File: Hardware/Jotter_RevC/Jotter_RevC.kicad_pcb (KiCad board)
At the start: 2 copper layers, 76.2 x 76.2 mm, 44 parts, among them CON1 SD_Card, P1 USB_A, P2 CONN_01X02, P3 CONN_01X02, Q1 BSS138, Q2 BSS138, SW1 SPST, U1 ATSAMD11D14A, U10 APA102C, U2 MCP73831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

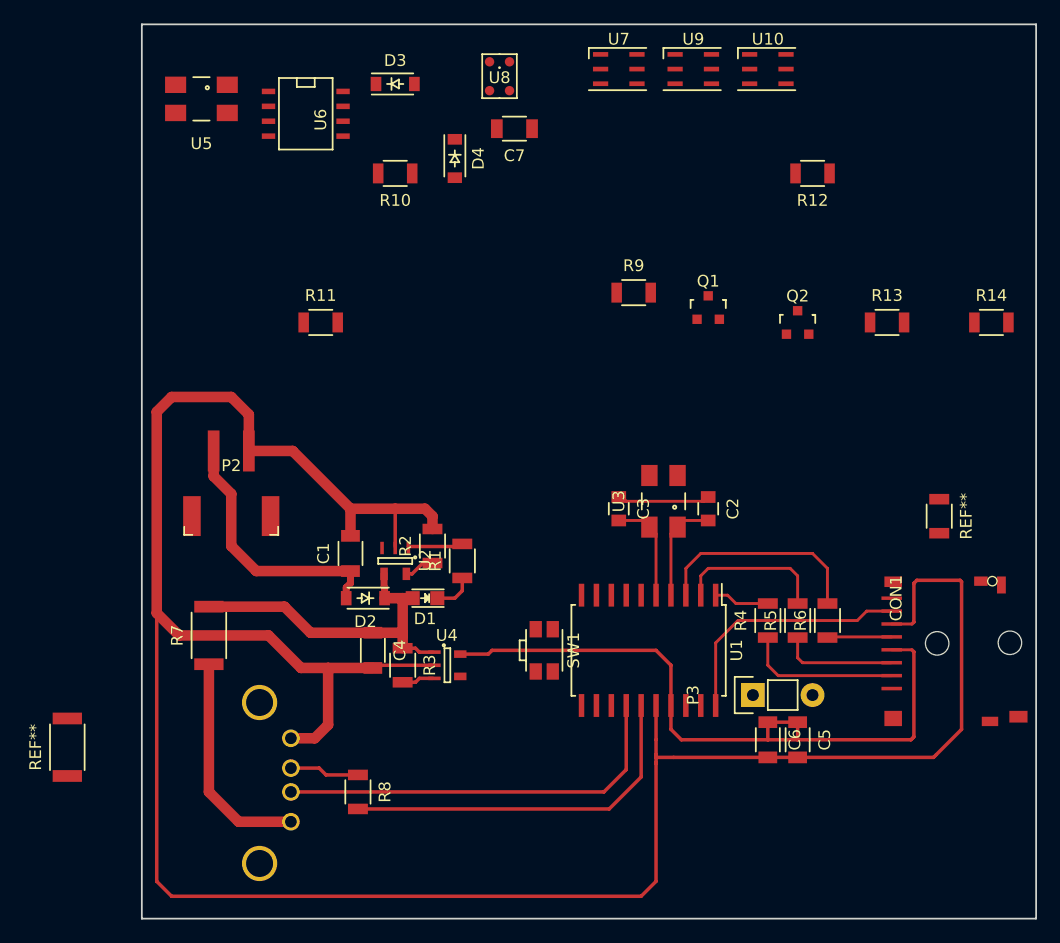
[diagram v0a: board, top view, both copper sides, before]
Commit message: added notes on which parts to select for development; added rought shematic and layout with most selected parts on the 3in by 3in layout to get a sense of component sizes.
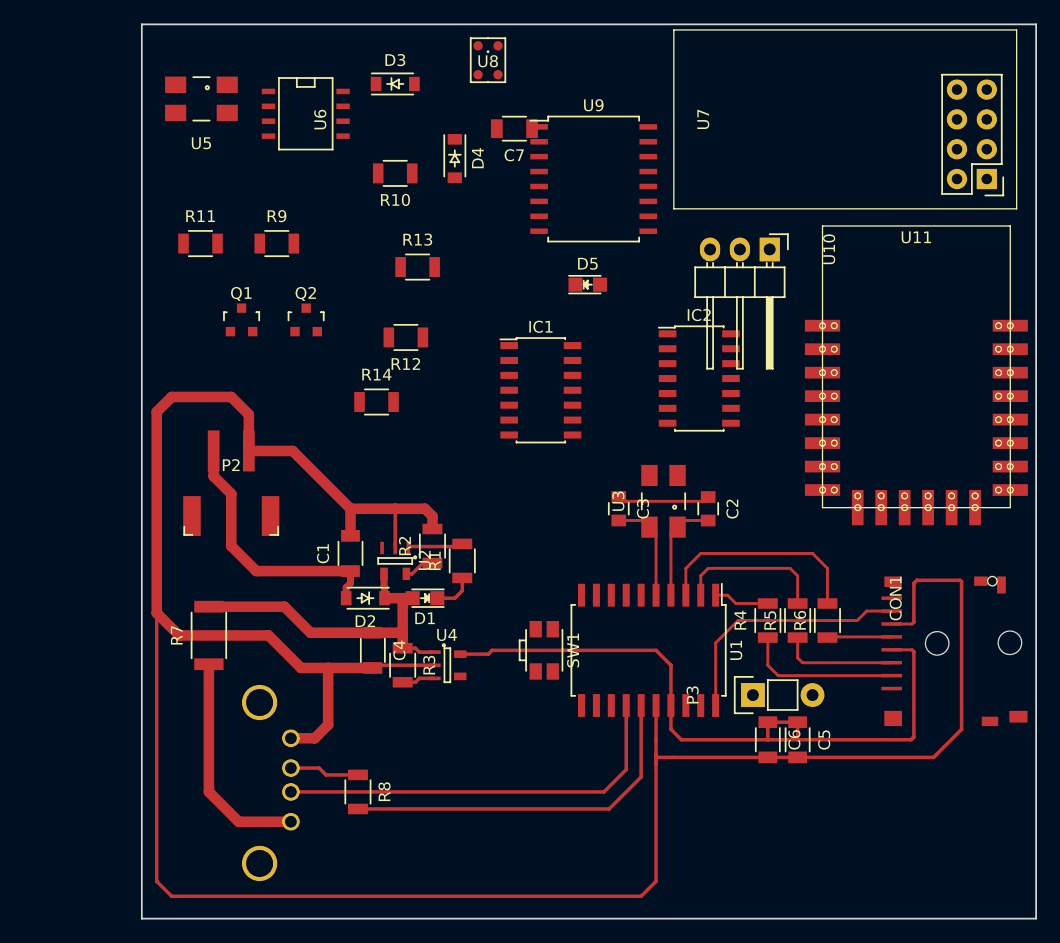
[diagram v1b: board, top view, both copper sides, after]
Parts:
- removed REF**: R_2010, Resistors_SMD:R_2010
- removed REF**: R_1206, Resistors_SMD:R_1206
- added D5: LED, LEDs:LED-0805, F.Cu at (101.5, 106.0)
- added IC1: ATTINY841-SSU, Housings_SOIC:SOIC-14_3.9x8.7mm_Pitch1.27mm, F.Cu at (97.5, 115.0)
- added IC2: ATTINY841-SSU, Housings_SOIC:SOIC-14_3.9x8.7mm_Pitch1.27mm, F.Cu at (111.0, 114.0)
- added U11: ESP8266-12E, MyKiCadParts:ESP8266-12E-80, F.Cu at (129.5, 109.0)
- U1: footprint MyKiCadParts:SOIC-20_7.5x12.8mm_Pitch1.27mm-80 -> Housings_SOIC:SOIC-20_7.5x12.8mm_Pitch1.27mm
- U10: value APA102C -> VS18388; footprint MyKiCadParts:LED_RGB_PLLC-6-80 -> Pin_Headers:Pin_Header_Angled_1x03
- U7: value APA102C -> NRF24L01+; footprint MyKiCadParts:LED_RGB_PLLC-6-80 -> MyKiCadParts:NRF24L01+
- U9: value APA102C -> DS3231; footprint MyKiCadParts:LED_RGB_PLLC-6-80 -> MyKiCadParts:SOIC-16-W-80
- moved R14 52.8 mm to (83.5, 116.0)
- moved Q2 41.9 mm to (77.5, 109.0)
- moved R13 40.3 mm to (87.0, 104.5)
- moved Q1 39.8 mm to (72.0, 109.0)
- moved R12 37.4 mm to (86.0, 110.5)
- moved U7 32.7 mm to (135.5, 97.0), turned to 180 degrees
- moved R9 30.7 mm to (75.0, 102.5)
- moved U10 15.4 mm to (117.0, 103.0), turned to 270 degrees
- moved U9 12.6 mm to (102.0, 97.0)
- moved R11 12.2 mm to (68.5, 102.5)
- moved U8 1.68 mm to (93.0, 85.0)
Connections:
- CON1 pad 1: Net-(CON1-Pad1) -> (no net)
- CON1 pad 8: Net-(CON1-Pad8) -> (no net)
- D4 pad 2: Net-(BT1-Pad1) -> (no net)
- U1 pad 12: TX -> (no net)
- U1 pad 13: RX -> (no net)
- U1 pad 19: PIN_03 -> (no net)
- U10 pad 1: Net-(U10-Pad1) -> (no net)
- U10 pad 2: Net-(U10-Pad2) -> (no net)
- U10 pad 3: GND -> (no net)
- U2 pad 3: Net-(U2-Pad3) -> (no net)
- U3 pad 2: Net-(U3-Pad2) -> (no net)
- U3 pad 3: Net-(U3-Pad3) -> (no net)
- U4 pad 4: Net-(U4-Pad4) -> (no net)
- U5 pad 2: Net-(U5-Pad2) -> (no net)
- U5 pad 3: Net-(U5-Pad3) -> (no net)
- U6 pad 3: Net-(U6-Pad3) -> (no net)
- U6 pad 7: Net-(U6-Pad7) -> (no net)
- U7 pad 1: APA_DATA -> (no net)
- U7 pad 2: APA_CLK -> (no net)
- U7 pad 3: GND -> (no net)
- U7 pad 4: V_USB -> (no net)
- U7 pad 5: Net-(U7-Pad5) -> (no net)
- U7 pad 6: Net-(U7-Pad6) -> (no net)
- U9 pad 1: Net-(U7-Pad6) -> (no net)
- U9 pad 2: Net-(U7-Pad5) -> (no net)
- U9 pad 3: GND -> (no net)
- U9 pad 4: V_USB -> (no net)
- U9 pad 5: Net-(U10-Pad2) -> (no net)
- U9 pad 6: Net-(U10-Pad1) -> (no net)
